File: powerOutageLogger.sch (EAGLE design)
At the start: 36 parts, among them J1 2.1MMJACKTHM, U1 ATmega328P, U2 78L05, U3 DS18B20, Y1 16MHz

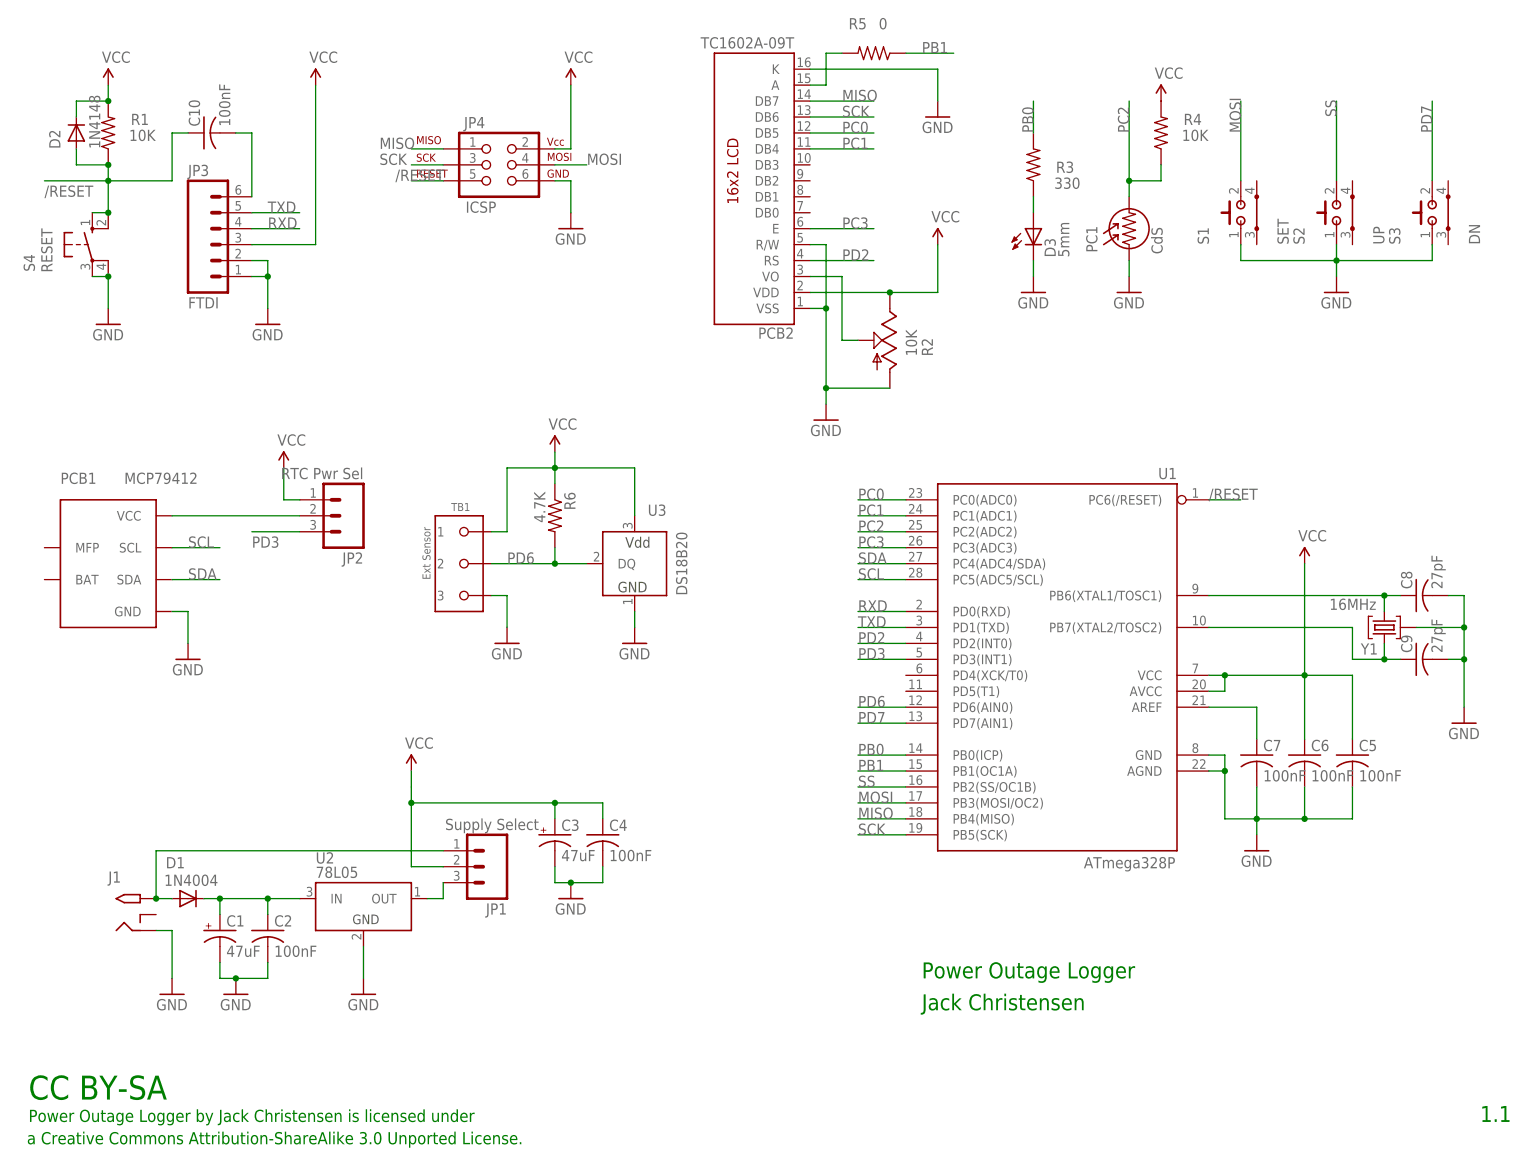
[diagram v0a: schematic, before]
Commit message: Improved board routing, added connection for RTC interrupt.
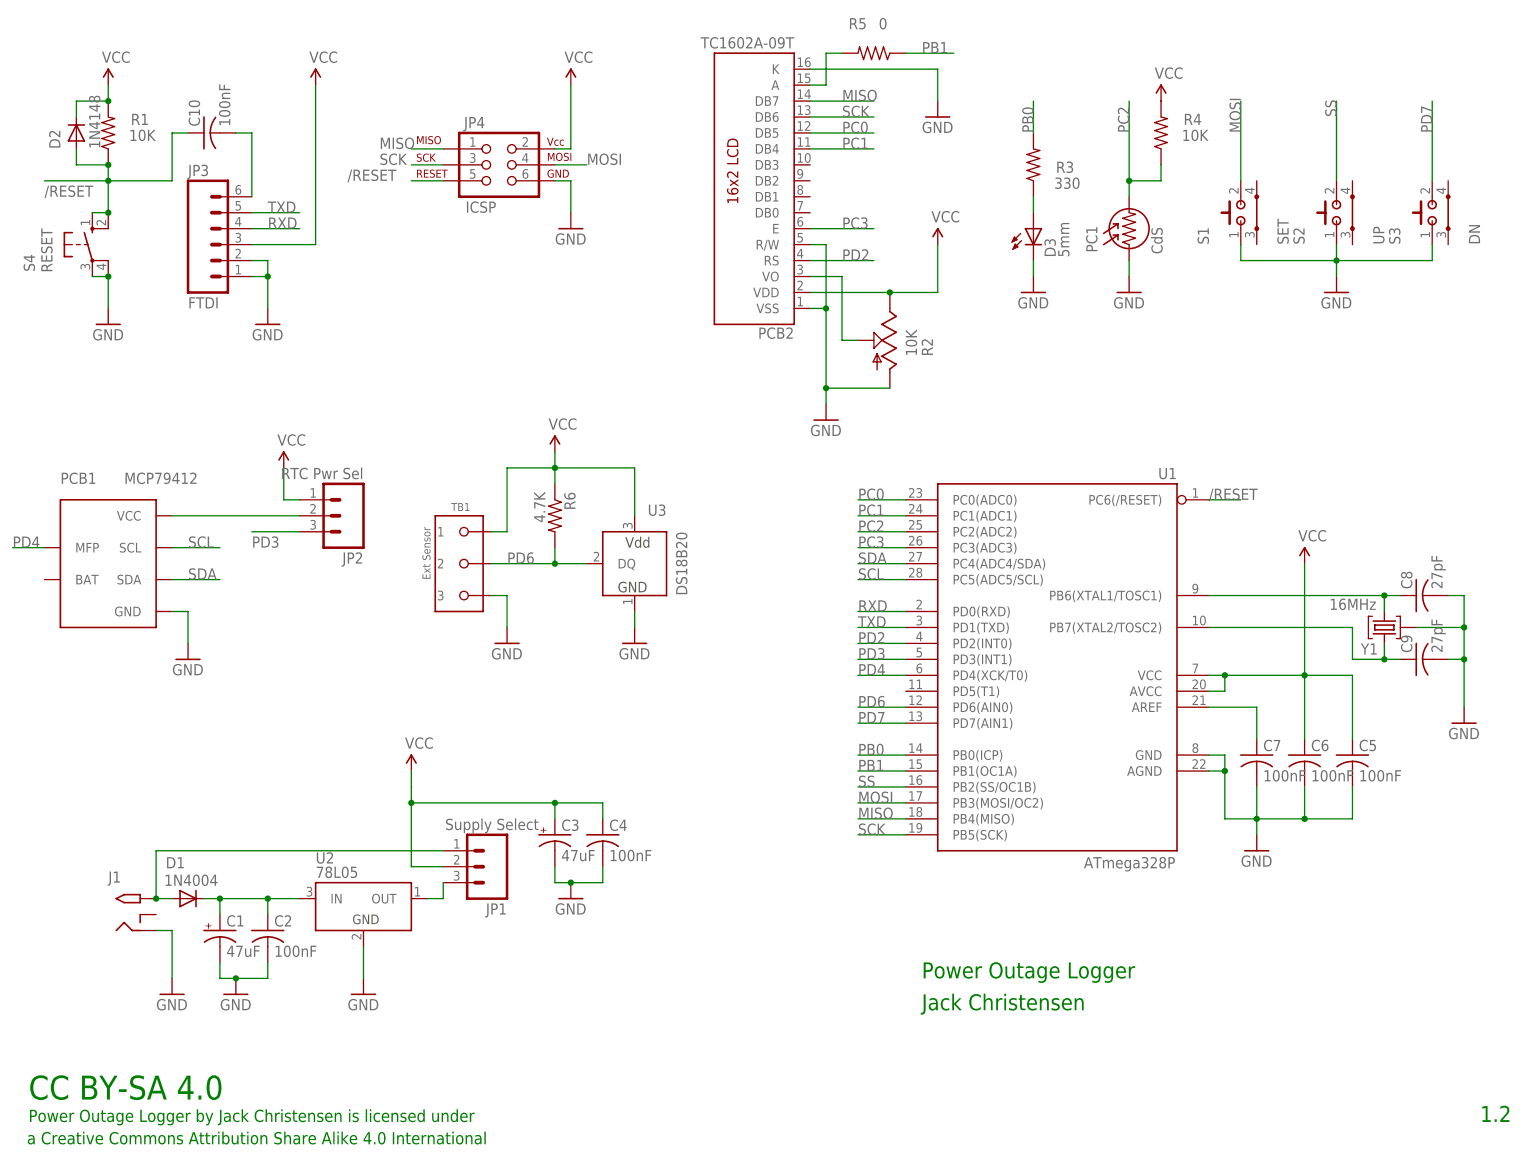
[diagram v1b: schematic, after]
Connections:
- new net PD4: PCB1.MFP, U1.PD4(XCK/T0)
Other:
- note added: "1.2"
- note added: "CC BY-SA 4.0"
- note added: "a Creative Commons Attribution Share Alike 4.0 International"
- note removed: "1.1"
- note removed: "CC BY-SA"
- note removed: "a Creative Commons Attribution-ShareAlike 3.0 Unported License."
